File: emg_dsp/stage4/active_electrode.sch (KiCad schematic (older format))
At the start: 24 parts

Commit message: notes, schematic mods, etc.
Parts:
- added C?: 10uf, 0603, symbol C
- added D? (x2): uclamp33, SOD-523, symbol ZENER
- added R?: 33, 0402, symbol R
- added TP?: V0, TP, symbol TP
- added U?: FCI_USB_B, FCI_USB_A, symbol FCI_USB_B
- C?: value 1nf -> 1.5nF
- R?: value 120k -> 170k
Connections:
- net OUT: now also R?.2
- net V+: now also D?.1 (A), U?.1 (VBUS)
- net V-: now also D?.2 (K), U?.4 (GND)
- net V0: now also D?.1 (A), D?.2 (K), TP?.1, U?.3 (D+), U?.s1 (shield), U?.s2 (shield); no longer TP?.1
- net at C?.2, R?.1, R?.2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: no longer R?.2
- net at C?.1, R?.2, U?.7 (OUT): now also C?.2
- new net: C?.1, R?.2
- new net: R?.1, U?.2 (D-)
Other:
- note added: "but it's easy!"
- note added: "e.g. those used in small portable mice"
- note added: "need to find some very thin USB cable for this"
- note added: "to reuse the USB A connector here.."
- note added: "yea, I know it's not a good idea"
- moved on the sheet: C?, R?, TP?, U?

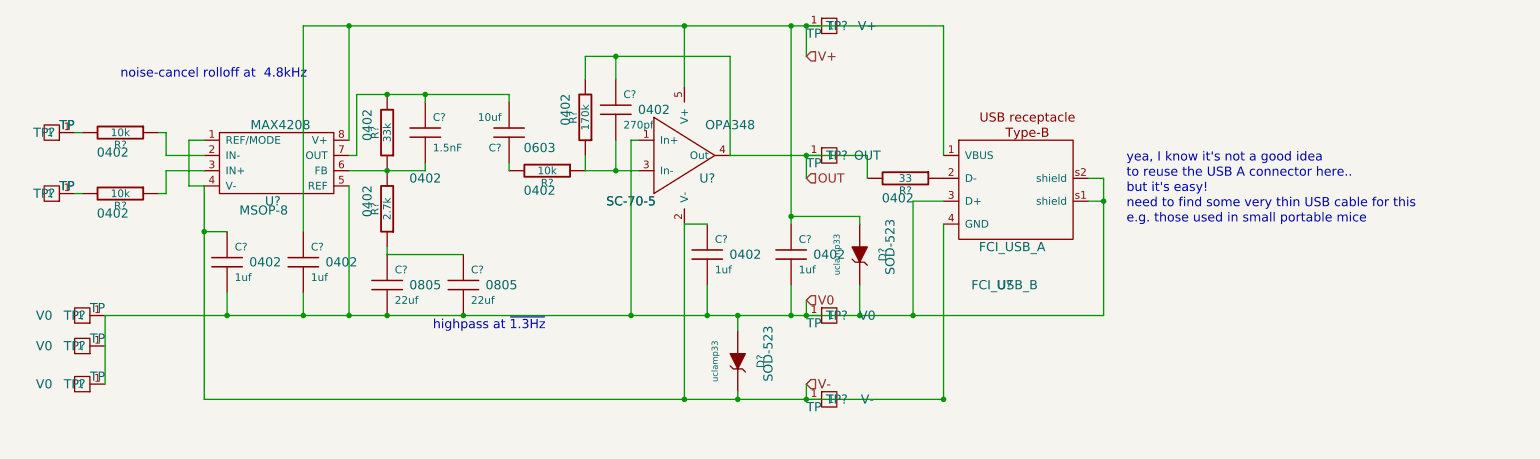
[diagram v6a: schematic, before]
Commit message: fixing the schematic with the help of the BOM.. trying to make the BOM simpler (and also making sure that U can actually buy all the parts on the board!)
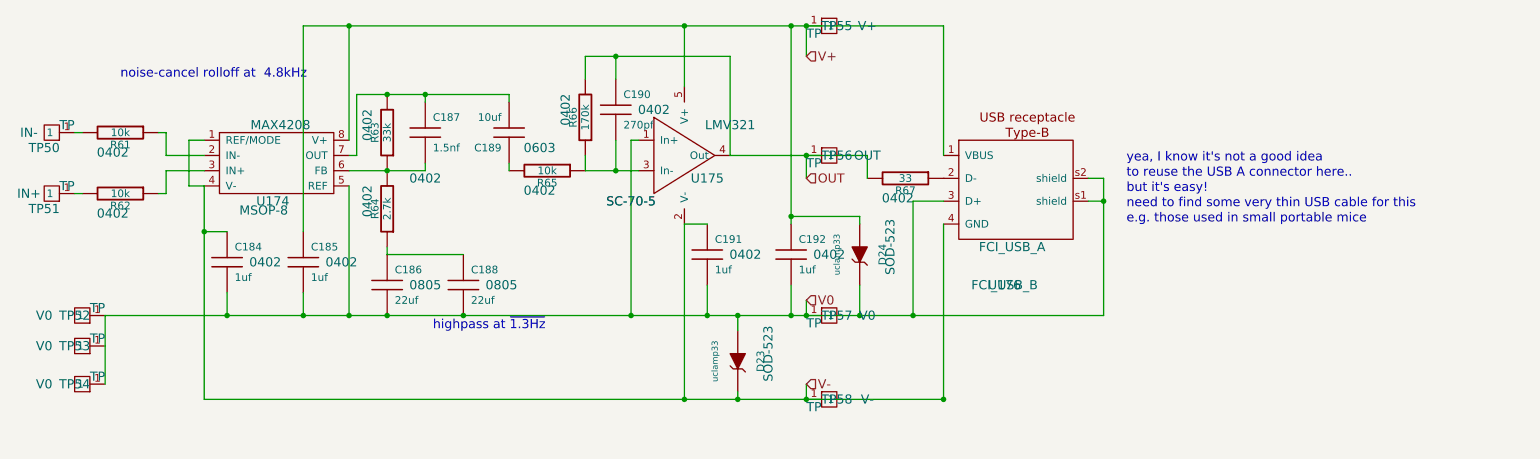
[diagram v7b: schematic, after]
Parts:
- C214: renamed from C?; value 1.5nF -> 1.5nf
- TP77: renamed from TP?; value TP -> IN-
- TP78: renamed from TP?; value TP -> IN+
- U184: renamed from U?; value OPA348 -> LMV321
- gave numbers to parts that had none: 26
